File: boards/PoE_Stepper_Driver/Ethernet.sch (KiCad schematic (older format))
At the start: 77 parts, among them J1 RJ45, Q1 NMOS_POE, Q10 NMOS_POE, Q3 NMOS_POE, Q4 NMOS_POE, Q5 NMOS_POE, Q6 NMOS_POE, Q7 NMOS_POE, Q8 NMOS_POE, Q9 NMOS_POE, U1 LT4321, U14 DP83848C, U2 LT4293, X1 SXO53C

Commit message: finished footprint assignment
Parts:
- C11, C13, C24, C25, C29, C33: footprint (none) -> Capacitor_SMD:C_0805_2012Metric_Pad1.15x1.40mm_HandSolder
- C4: footprint (none) -> Capacitor_SMD:CP_Elec_8x10.5
- JP1, JP2, JP3, JP4: footprint (none) -> Connector_PinHeader_2.54mm:PinHeader_1x02_P2.54mm_Vertical
- R19: footprint Resistor_SMD:R_0603_1608Metric_Pad1.05x0.95mm_HandSolder -> Resistor_SMD:R_0805_2012Metric_Pad1.15x1.40mm_HandSolder
- R20, R21, R22, R30, R31, R32, R33, R34, R35, R36: footprint (none) -> Resistor_SMD:R_0805_2012Metric_Pad1.15x1.40mm_HandSolder
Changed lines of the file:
@@
 F 0 "C4" H 6463 4521 50  0000 L CNN
 F 1 "22uF" H 6463 4430 50  0000 L CNN
-F 2 "" H 6375 4475 50  0001 C CNN
+F 2 "Capacitor_SMD:CP_Elec_8x10.5" H 6375 4475 50  0001 C CNN
 F 3 "~" H 6375 4475 50  0001 C CNN
 	1    6375 4475
@@
 F 0 "JP1" H 1300 7343 50  0000 C CNN
 F 1 "Jumper_NO_Small" H 1300 7344 50  0001 C CNN
-F 2 "" H 1300 7250 50  0001 C CNN
+F 2 "Connector_PinHeader_2.54mm:PinHeader_1x02_P2.54mm_Vertical" H 1300 7250 50  0001 C CNN
 F 3 "~" H 1300 7250 50  0001 C CNN
 	1    1300 7250
@@
 F 0 "JP3" H 1300 7668 50  0000 C CNN
 F 1 "Jumper_NO_Small" H 1300 7669 50  0001 C CNN
-F 2 "" H 1300 7575 50  0001 C CNN
+F 2 "Connector_PinHeader_2.54mm:PinHeader_1x02_P2.54mm_Vertical" H 1300 7575 50  0001 C CNN
 F 3 "~" H 1300 7575 50  0001 C CNN
 	1    1300 7575
@@
 F 0 "JP2" H 1650 7343 50  0000 C CNN
 F 1 "Jumper_NO_Small" H 1650 7344 50  0001 C CNN
-F 2 "" H 1650 7250 50  0001 C CNN
+F 2 "Connector_PinHeader_2.54mm:PinHeader_1x02_P2.54mm_Vertical" H 1650 7250 50  0001 C CNN
 F 3 "~" H 1650 7250 50  0001 C CNN
 	1    1650 7250
@@
 F 0 "JP4" H 1550 7668 50  0000 C CNN
 F 1 "Jumper_NO_Small" H 1550 7669 50  0001 C CNN
-F 2 "" H 1550 7575 50  0001 C CNN
+F 2 "Connector_PinHeader_2.54mm:PinHeader_1x02_P2.54mm_Vertical" H 1550 7575 50  0001 C CNN
 F 3 "~" H 1550 7575 50  0001 C CNN
 	1    1550 7575
@@
 F 0 "R30" V 8025 4825 50  0000 C CNN
 F 1 "2.2k" V 8000 5025 50  0000 C CNN
-F 2 "" H 8075 4925 50  0001 C CNN
+F 2 "Resistor_SMD:R_0805_2012Metric_Pad1.15x1.40mm_HandSolder" H 8075 4925 50  0001 C CNN
 F 3 "~" H 8075 4925 50  0001 C CNN
 	1    8075 4925
@@
 F 0 "R31" V 8125 4900 50  0000 C CNN
 F 1 "2.2k" V 8025 5175 50  0000 C CNN
-F 2 "" H 8075 5025 50  0001 C CNN
+F 2 "Resistor_SMD:R_0805_2012Metric_Pad1.15x1.40mm_HandSolder" H 8075 5025 50  0001 C CNN
 F 3 "~" H 8075 5025 50  0001 C CNN
 	1    8075 5025
@@
 F 0 "R32" V 8175 5125 50  0000 C CNN
 F 1 "4.7k" V 8250 5125 50  0000 C CNN
-F 2 "" H 8100 5175 50  0001 C CNN
+F 2 "Resistor_SMD:R_0805_2012Metric_Pad1.15x1.40mm_HandSolder" H 8100 5175 50  0001 C CNN
 F 3 "~" H 8100 5175 50  0001 C CNN
 	1    8100 5175
@@
 F 0 "R20" V 7950 5125 50  0000 C CNN
 F 1 "150" V 8025 5125 50  0000 C CNN
-F 2 "" H 7875 5175 50  0001 C CNN
+F 2 "Resistor_SMD:R_0805_2012Metric_Pad1.15x1.40mm_HandSolder" H 7875 5175 50  0001 C CNN
 F 3 "~" H 7875 5175 50  0001 C CNN
 	1    7875 5175
@@
 F 0 "R19" V 7725 5125 50  0000 C CNN
 F 1 "18" V 7800 5125 50  0000 C CNN
-F 2 "Resistor_SMD:R_0603_1608Metric_Pad1.05x0.95mm_HandSolder" H 7650 5175 50  0001 C CNN
+F 2 "Resistor_SMD:R_0805_2012Metric_Pad1.15x1.40mm_HandSolder" H 7650 5175 50  0001 C CNN
 F 3 "~" H 7650 5175 50  0001 C CNN
 	1    7650 5175
@@
 F 0 "C29" H 8575 6125 50  0000 L CNN
 F 1 "10uF" H 8575 5975 50  0000 L CNN
-F 2 "" H 8550 6050 50  0001 C CNN
+F 2 "Capacitor_SMD:C_0805_2012Metric_Pad1.15x1.40mm_HandSolder" H 8550 6050 50  0001 C CNN
 F 3 "~" H 8550 6050 50  0001 C CNN
 	1    8550 6050
@@
 F 0 "R21" H 7850 2900 50  0000 C CNN
 F 1 "18" H 7850 2825 50  0000 C CNN
-F 2 "" H 7950 2875 50  0001 C CNN
+F 2 "Resistor_SMD:R_0805_2012Metric_Pad1.15x1.40mm_HandSolder" H 7950 2875 50  0001 C CNN
 F 3 "~" H 7950 2875 50  0001 C CNN
 	1    7950 2875
@@
 F 0 "R33" H 8050 2900 50  0000 C CNN
 F 1 "18" H 8050 2825 50  0000 C CNN
-F 2 "" H 8150 2875 50  0001 C CNN
+F 2 "Resistor_SMD:R_0805_2012Metric_Pad1.15x1.40mm_HandSolder" H 8150 2875 50  0001 C CNN
 F 3 "~" H 8150 2875 50  0001 C CNN
 	1    8150 2875
@@
 F 0 "R22" H 7850 3600 50  0000 C CNN
 F 1 "18" H 7850 3525 50  0000 C CNN
-F 2 "" H 7950 3575 50  0001 C CNN
+F 2 "Resistor_SMD:R_0805_2012Metric_Pad1.15x1.40mm_HandSolder" H 7950 3575 50  0001 C CNN
 F 3 "~" H 7950 3575 50  0001 C CNN
 	1    7950 3575
@@
 F 0 "R34" H 8050 3600 50  0000 C CNN
 F 1 "18" H 8050 3525 50  0000 C CNN
-F 2 "" H 8150 3575 50  0001 C CNN
+F 2 "Resistor_SMD:R_0805_2012Metric_Pad1.15x1.40mm_HandSolder" H 8150 3575 50  0001 C CNN
 F 3 "~" H 8150 3575 50  0001 C CNN
 	1    8150 3575
@@
 F 0 "C25" H 7467 3521 50  0000 L CNN
 F 1 "0.1uF" H 7467 3430 50  0000 L CNN
-F 2 "" H 7375 3475 50  0001 C CNN
+F 2 "Capacitor_SMD:C_0805_2012Metric_Pad1.15x1.40mm_HandSolder" H 7375 3475 50  0001 C CNN
 F 3 "~" H 7375 3475 50  0001 C CNN
 	1    7375 3475
@@
 F 0 "C24" H 7467 2921 50  0000 L CNN
 F 1 "0.1uF" H 7467 2830 50  0000 L CNN
-F 2 "" H 7375 2875 50  0001 C CNN
+F 2 "Capacitor_SMD:C_0805_2012Metric_Pad1.15x1.40mm_HandSolder" H 7375 2875 50  0001 C CNN
 F 3 "~" H 7375 2875 50  0001 C CNN
 	1    7375 2875
@@
 F 0 "R35" V 10475 4400 50  0000 C CNN
 F 1 "2.2k" V 10475 4200 50  0000 C CNN
-F 2 "" H 10550 4325 50  0001 C CNN
+F 2 "Resistor_SMD:R_0805_2012Metric_Pad1.15x1.40mm_HandSolder" H 10550 4325 50  0001 C CNN
 F 3 "~" H 10550 4325 50  0001 C CNN
 	1    10550 4325
@@
 F 0 "R36" V 10625 4500 50  0000 C CNN
 F 1 "2.2k" V 10625 4300 50  0000 C CNN
-F 2 "" H 10550 4425 50  0001 C CNN
+F 2 "Resistor_SMD:R_0805_2012Metric_Pad1.15x1.40mm_HandSolder" H 10550 4425 50  0001 C CNN
 F 3 "~" H 10550 4425 50  0001 C CNN
 	1    10550 4425
@@
 F 0 "C13" V 4725 1950 50  0000 L CNN
 F 1 "0.1uF" V 4825 1925 50  0000 L CNN
-F 2 "" H 4775 1900 50  0001 C CNN
+F 2 "Capacitor_SMD:C_0805_2012Metric_Pad1.15x1.40mm_HandSolder" H 4775 1900 50  0001 C CNN
 F 3 "~" H 4775 1900 50  0001 C CNN
 	1    4775 1900
@@
 F 0 "C11" V 4725 1725 50  0000 L CNN
 F 1 "0.1uF" V 4825 1725 50  0000 L CNN
-F 2 "" H 4775 1700 50  0001 C CNN
+F 2 "Capacitor_SMD:C_0805_2012Metric_Pad1.15x1.40mm_HandSolder" H 4775 1700 50  0001 C CNN
 F 3 "~" H 4775 1700 50  0001 C CNN
 	1    4775 1700
@@
 F 0 "C33" H 10675 2225 50  0000 L CNN
 F 1 "10nF" H 10675 2075 50  0000 L CNN
-F 2 "" H 10650 2150 50  0001 C CNN
+F 2 "Capacitor_SMD:C_0805_2012Metric_Pad1.15x1.40mm_HandSolder" H 10650 2150 50  0001 C CNN
 F 3 "~" H 10650 2150 50  0001 C CNN
 	1    10650 2150

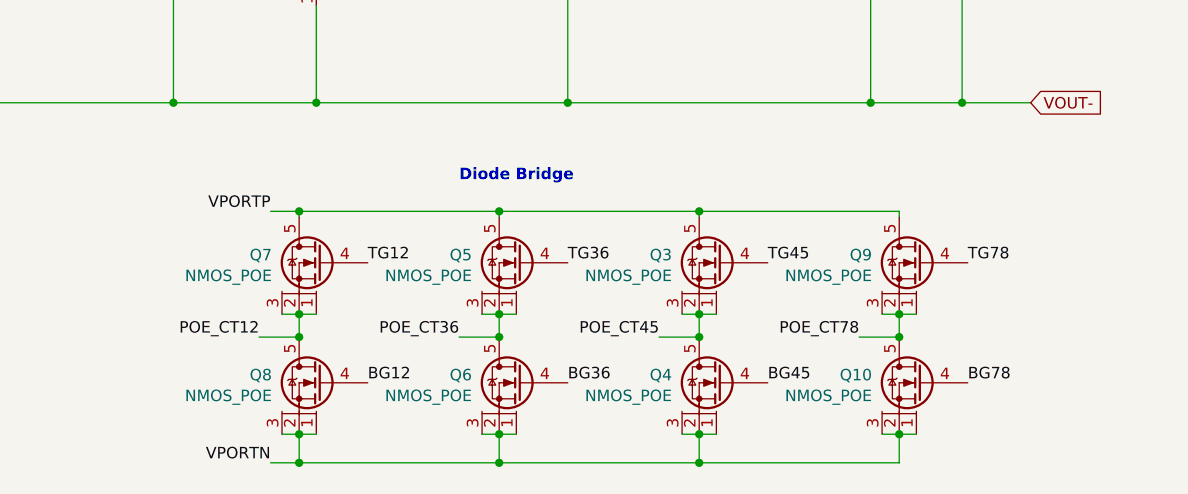
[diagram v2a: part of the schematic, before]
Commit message: added working blink code
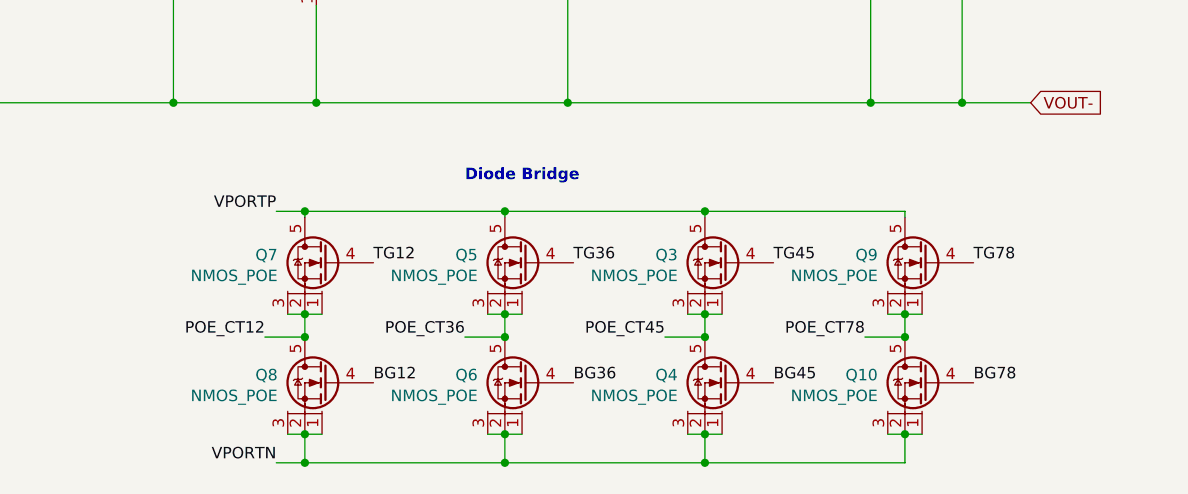
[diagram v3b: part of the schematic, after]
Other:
- moved on the sheet: Q10, Q3, Q4, Q5, Q6, Q7, Q8, Q9

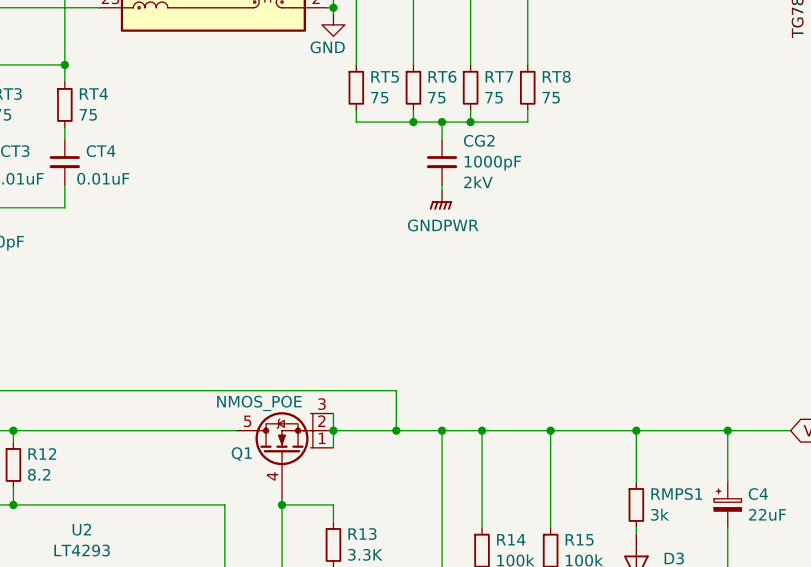
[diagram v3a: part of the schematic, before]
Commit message: writing to 429 is working
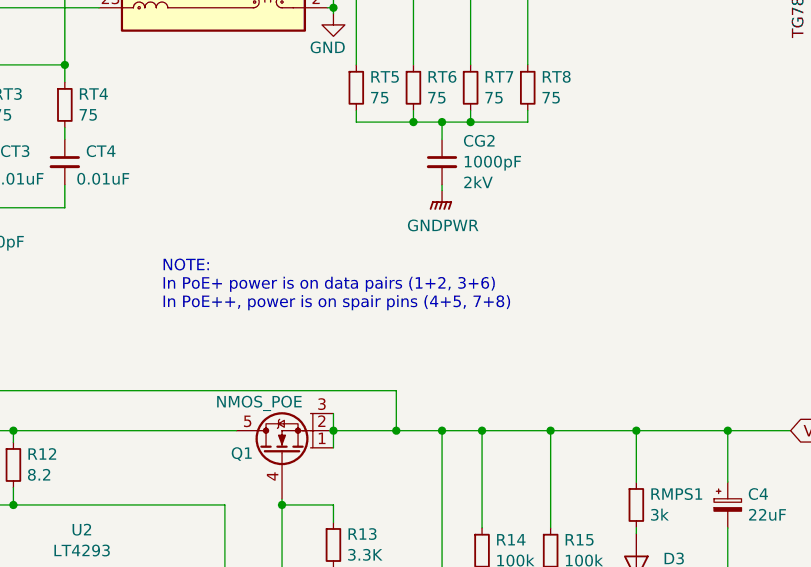
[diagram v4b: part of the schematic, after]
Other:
- note added: "NOTE: \nIn PoE+ power is on data pairs (1+2, 3+6)\nIn PoE++, power is on spair pins (4+5, 7+8)"
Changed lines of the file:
@@
 	-1   0    0    -1
 $EndComp
+Text Notes 3900 3625 0    50   ~ 0
+NOTE: \nIn PoE+ power is on data pairs (1+2, 3+6)\nIn PoE++, power is on spair pins (4+5, 7+8)
 $EndSCHEMATC
